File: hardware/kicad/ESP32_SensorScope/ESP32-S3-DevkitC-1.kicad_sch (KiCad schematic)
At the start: 1 part, among them U1 ESP32-S3-DevKitC

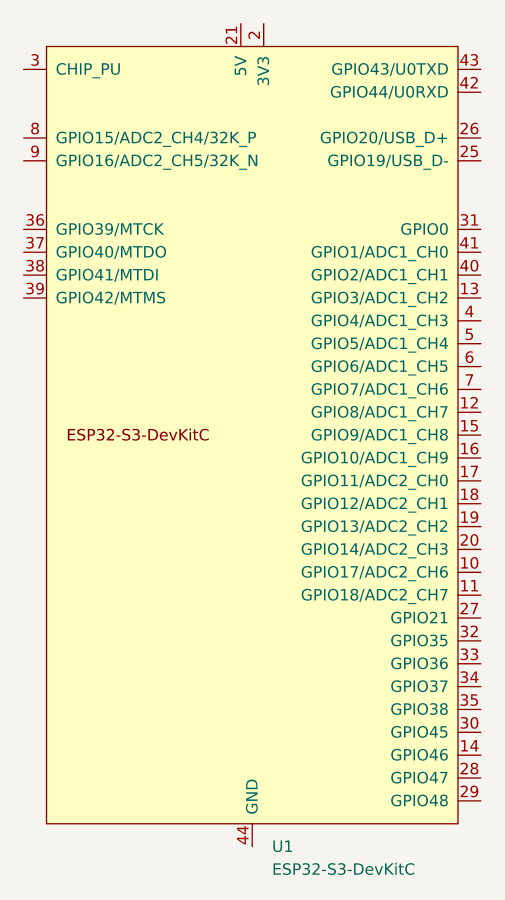
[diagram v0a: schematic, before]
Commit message: Added serial interfases
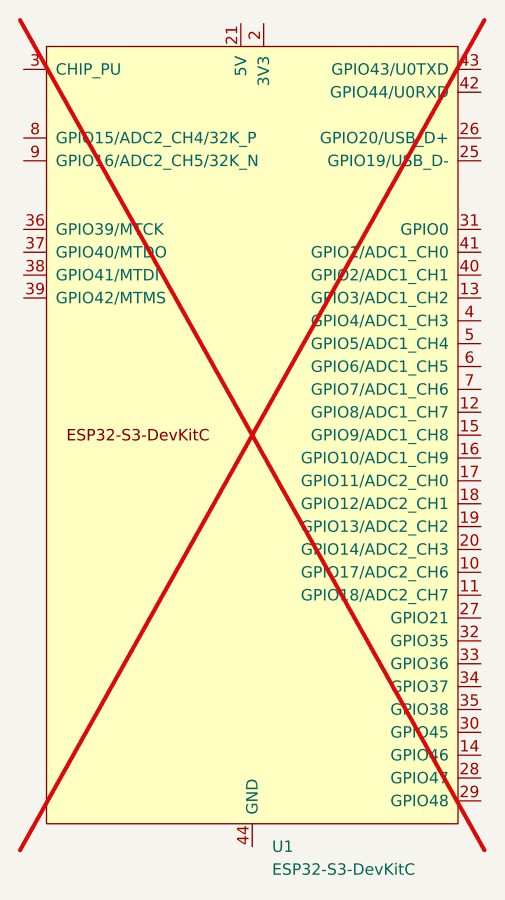
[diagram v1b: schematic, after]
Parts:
- U1: now not fitted; now left out of the parts list
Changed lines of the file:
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@@
 		(unit 1)
 		(exclude_from_sim no)
-		(in_bom yes)
-		(on_board yes)
-		(dnp no)
+		(in_bom no)
+		(on_board no)
+		(dnp yes)
 		(fields_autoplaced yes)
 		(property "Reference" "U1"
